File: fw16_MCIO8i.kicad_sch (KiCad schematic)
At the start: 12 parts

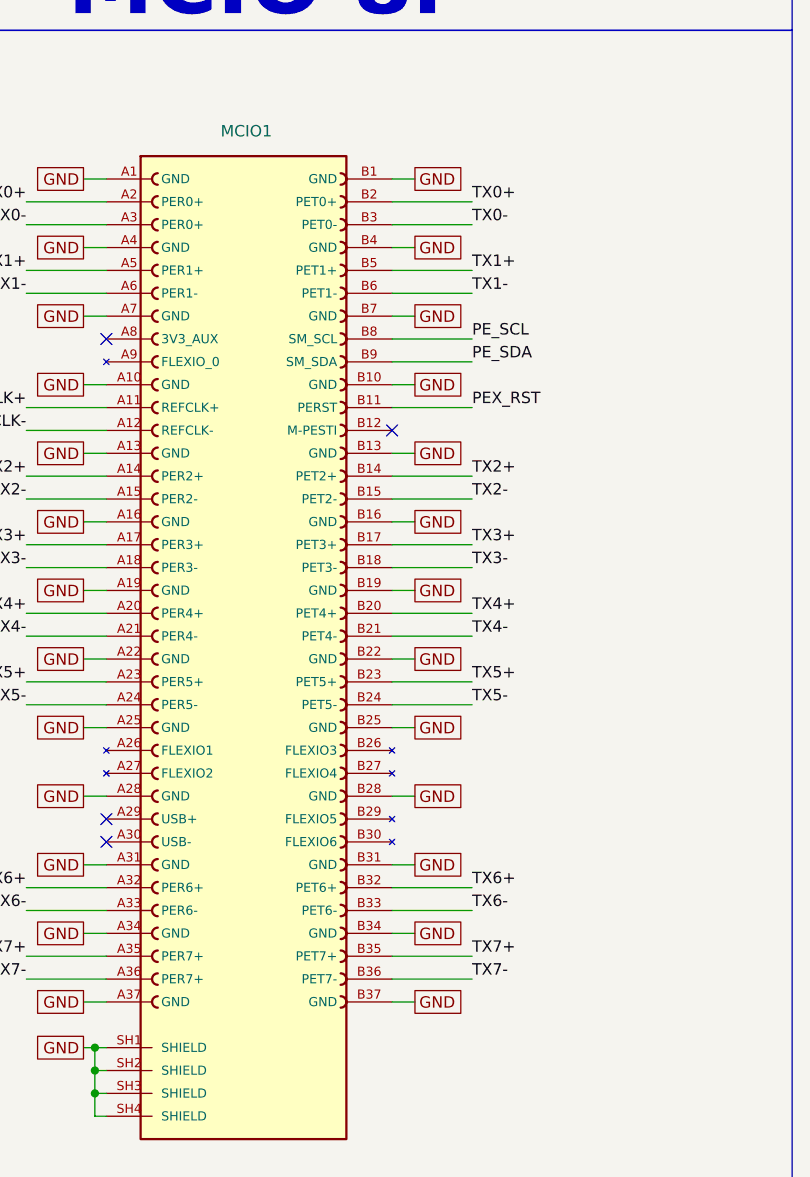
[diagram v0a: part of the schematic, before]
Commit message: Rerouted fxbeam
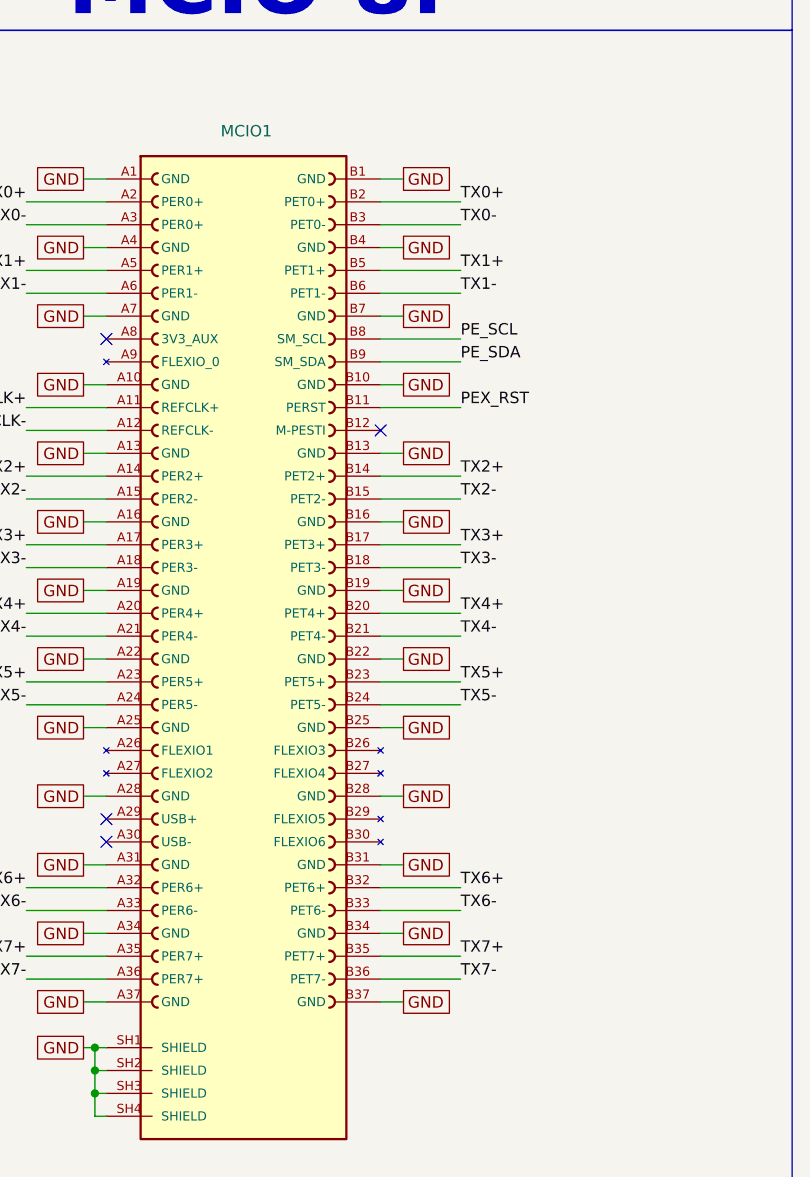
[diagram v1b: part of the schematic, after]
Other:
- moved on the sheet: MCIO1

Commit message: Fixed errors
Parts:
- C1: MPN (none) -> CL05A105KA5NQNC; PROD_ID (none) -> CAP-25565; Voltage (none) -> 16V
- EEPROM1: MPN (none) -> M24C32-FDW6TP
- FAN_L1, FAN_R1: CREATOR (none) -> ANA
- R1, R2: MPN (none) -> 0402WGF3303TCE; PROD_ID (none) -> RES-15407
- R50, R51: MPN (none) -> 0402WGF1002TCE; PROD_ID (none) -> RES-25567
- TP_POWER1: renamed from TP5; now left out of the parts list
- TP_SIGNAL1: renamed from TP3; now left out of the parts list
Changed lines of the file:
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@@
+		(polyline
+			(pts
+				(xy 76.2 162.56) (xy 78.74 162.56) (xy 78.74 184.15) (xy 76.2 184.15)
+			)
+			(stroke
+				(width 0)
+				(type dash)
+			)
+			(fill
+				(type none)
+			)
+		)
+	)
+	(rule_area
+		(polyline
+			(pts
+				(xy 34.29 245.11) (xy 36.83 245.11) (xy 36.83 247.65) (xy 34.29 247.65)
+			)
+			(stroke
+				(width 0)
+				(type dash)
+			)
+			(fill
+				(type none)
+			)
+		)
+	)
+	(rule_area
 		(polyline
 			(pts
 				(xy 76.2 40.64) (xy 76.2 140.97) (xy 78.74 140.97) (xy 78.74 40.64)
+			)
+			(stroke
+				(width 0)
+				(type dash)
+			)
+			(fill
+				(type none)
+			)
+		)
+	)
+	(rule_area
+		(polyline
+			(pts
+				(xy 76.2 241.3) (xy 78.74 241.3) (xy 78.74 278.13) (xy 76.2 278.13)
 			)
 			(stroke
@@
 			(pts
 				(xy 33.02 113.03) (xy 35.56 113.03) (xy 34.29 231.14) (xy 31.75 231.14)
-			)
-			(stroke
-				(width 0)
-				(type dash)
-			)
-			(fill
-				(type none)
-			)
-		)
-	)
-	(rule_area
-		(polyline
-			(pts
-				(xy 76.2 241.3) (xy 78.74 241.3) (xy 78.74 278.13) (xy 76.2 278.13)
-			)
-			(stroke
-				(width 0)
-				(type dash)
-			)
-			(fill
-				(type none)
-			)
-		)
-	)
-	(rule_area
-		(polyline
-			(pts
-				(xy 34.29 245.11) (xy 36.83 245.11) (xy 36.83 247.65) (xy 34.29 247.65)
-			)
-			(stroke
-				(width 0)
-				(type dash)
-			)
-			(fill
-				(type none)
-			)
-		)
-	)
-	(rule_area
-		(polyline
-			(pts
-				(xy 76.2 162.56) (xy 78.74 162.56) (xy 78.74 184.15) (xy 76.2 184.15)
 			)
 			(stroke
@@
 		(property "Temperature Coefficient" "±100ppm/°C"
 			(at 264.16 40.64 0)
+			(hide yes)
+			(effects
+				(font
+					(size 1.27 1.27)
+				)
+			)
+		)
+		(property "PROD_ID" "RES-25567"
+			(at 264.16 40.64 0)
+			(hide yes)
+			(effects
+				(font
+					(size 1.27 1.27)
+				)
+			)
+		)
+		(property "MPN" "0402WGF1002TCE"
+			(at 264.16 44.45 0)
 			(hide yes)
 			(effects
@@
 			)
 		)
+		(property "PROD_ID" "RES-25567"
+			(at 269.24 43.18 0)
+			(hide yes)
+			(effects
+				(font
+					(size 1.27 1.27)
+				)
+			)
+		)
+		(property "MPN" "0402WGF1002TCE"
+			(at 269.24 45.72 0)
+			(hide yes)
+			(effects
+				(font
+					(size 1.27 1.27)
+				)
+			)
+		)
 		(pin "1"
 		)
@@
 			)
 		)
+		(property "MPN" "M24C32-FDW6TP"
+			(at 219.71 48.26 0)
+			(hide yes)
+			(effects
+				(font
+					(size 1.27 1.27)
+				)
+			)
+		)
 		(pin "7"
 		)
@@
 		(unit 1)
 		(exclude_from_sim no)
-		(in_bom yes)
+		(in_bom no)
 		(on_board yes)
 		(dnp no)
-		(property "Reference" "TP3"
+		(property "Reference" "TP_SIGNAL1"
 			(at 36.068 102.87 0)
 			(effects
@@
 		(property "Value" "TestPoint_Small"
 			(at 32.512 101.092 0)
+			(hide yes)
 			(effects
 				(font
@@
 			(project "fw16_MCIO8i"
 				(path "/50f5fd03-67f8-43d1-8bfe-dca2cf908bf0"
-					(reference "TP3")
+					(reference "TP_SIGNAL1")
 					(unit 1)
 				)
@@
 			)
 		)
+		(property "CREATOR" "ANA"
+			(at 173.99 38.1 0)
+			(hide yes)
+			(effects
+				(font
+					(size 1.27 1.27)
+				)
+			)
+		)
+		(property "VERIFIER" ""
+			(at 173.99 38.1 0)
+			(hide yes)
+			(effects
+				(font
+					(size 1.27 1.27)
+				)
+			)
+		)
 		(pin "1"
 		)
@@
 		(property "MPN" "609-F33D-1A7H1-E7C04CT-ND"
 			(at 139.954 60.198 0)
+			(hide yes)
+			(effects
+				(font
+					(size 1.27 1.27)
+				)
+			)
+		)
+		(property "CREATOR" "ANA"
+			(at 139.7 38.1 0)
+			(hide yes)
+			(effects
+				(font
+					(size 1.27 1.27)
+				)
+			)
+		)
+		(property "VERIFIER" ""
+			(at 139.7 38.1 0)
 			(hide yes)
 			(effects
@@
 			)
 		)
+		(property "PROD_ID" "RES-15407"
+			(at 35.56 273.05 0)
+			(hide yes)
+			(effects
+				(font
+					(size 1.27 1.27)
+				)
+			)
+		)
+		(property "MPN" "0402WGF3303TCE"
+			(at 35.56 273.05 0)
+			(hide yes)
+			(effects
+				(font
+					(size 1.27 1.27)
+				)
+			)
+		)
 		(pin "1"
 		)
@@
 			)
 		)
+		(property "PROD_ID" "RES-15407"
+			(at 27.94 100.33 0)
+			(hide yes)
+			(effects
+				(font
+					(size 1.27 1.27)
+				)
+			)
+		)
+		(property "MPN" "0402WGF3303TCE"
+			(at 27.94 100.33 0)
+			(hide yes)
+			(effects
+				(font
+					(size 1.27 1.27)
+				)
+			)
+		)
 		(pin "1"
 		)
@@
 		(unit 1)
 		(exclude_from_sim no)
-		(in_bom yes)
+		(in_bom no)
 		(on_board yes)
 		(dnp no)
-		(property "Reference" "TP5"
-			(at 33.02 264.16 0)
+		(property "Reference" "TP_POWER1"
+			(at 31.242 266.7 0)
 			(effects
 				(font
@@
 		(property "Value" "TestPoint_Small"
 			(at 33.02 265.938 0)
+			(hide yes)
 			(effects
 				(font
@@
 			(project "fw16_MCIO8i"
 				(path "/50f5fd03-67f8-43d1-8bfe-dca2cf908bf0"
-					(reference "TP5")
+					(reference "TP_POWER1")
 					(unit 1)
 				)
@@
 		(on_board yes)
 		(dnp no)
-		(fields_autoplaced yes)
 		(property "Reference" "C1"
 			(at 246.38 34.2899 0)
@@
 			(hide yes)
 			(effects
+				(font
+					(size 1.27 1.27)
+				)
+			)
+		)
+		(property "PROD_ID" "CAP-25565"
+			(at 243.84 36.83 0)
+			(hide yes)
+			(effects
+				(font
+					(size 1.27 1.27)
+				)
+			)
+		)
+		(property "Voltage" "16V"
+			(at 243.84 36.83 0)
+			(hide yes)
+			(effects
+				(font
+					(size 1.27 1.27)
+				)
+			)
+		)
+		(property "MPN" "CL05A105KA5NQNC"
+			(at 248.92 41.91 0)
+			(hide yes)
+			(effects

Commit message: New routing
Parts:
- C1: MPN CL05A105KA5NQNC -> (none); PROD_ID CAP-25565 -> (none); Voltage 16V -> (none)
- EEPROM1: MPN M24C32-FDW6TP -> (none); now in the parts list
- IN1: renamed from FXBEAM1; value IN -> FXBEAM
- R1, R2: MPN 0402WGF3303TCE -> (none); PROD_ID RES-15407 -> (none)
- R50, R51: MPN 0402WGF1002TCE -> (none); PROD_ID RES-25567 -> (none)
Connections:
- net I2C_SCL: now also IN1.PD3 (I2C_DAT_ALW); no longer IN1.PF2 (I2C_INT_ALW)
- net I2C_SDA: now also IN1.PC3 (I2C_CLK_ALW); no longer IN1.PD3 (I2C_DAT_ALW)
- net PEX_RST: now also IN1.PF3 (PEX1_RST); no longer IN1.SA5 (PEX_RST#)
- net PE_SCL: now also IN1.PK1 (DDS_SDA); no longer IN1.PG3 (I2C_DAT_VS)
- net PE_SDA: now also IN1.PL2 (DDS_CLK); no longer IN1.PG2 (I2C_INT_VS)

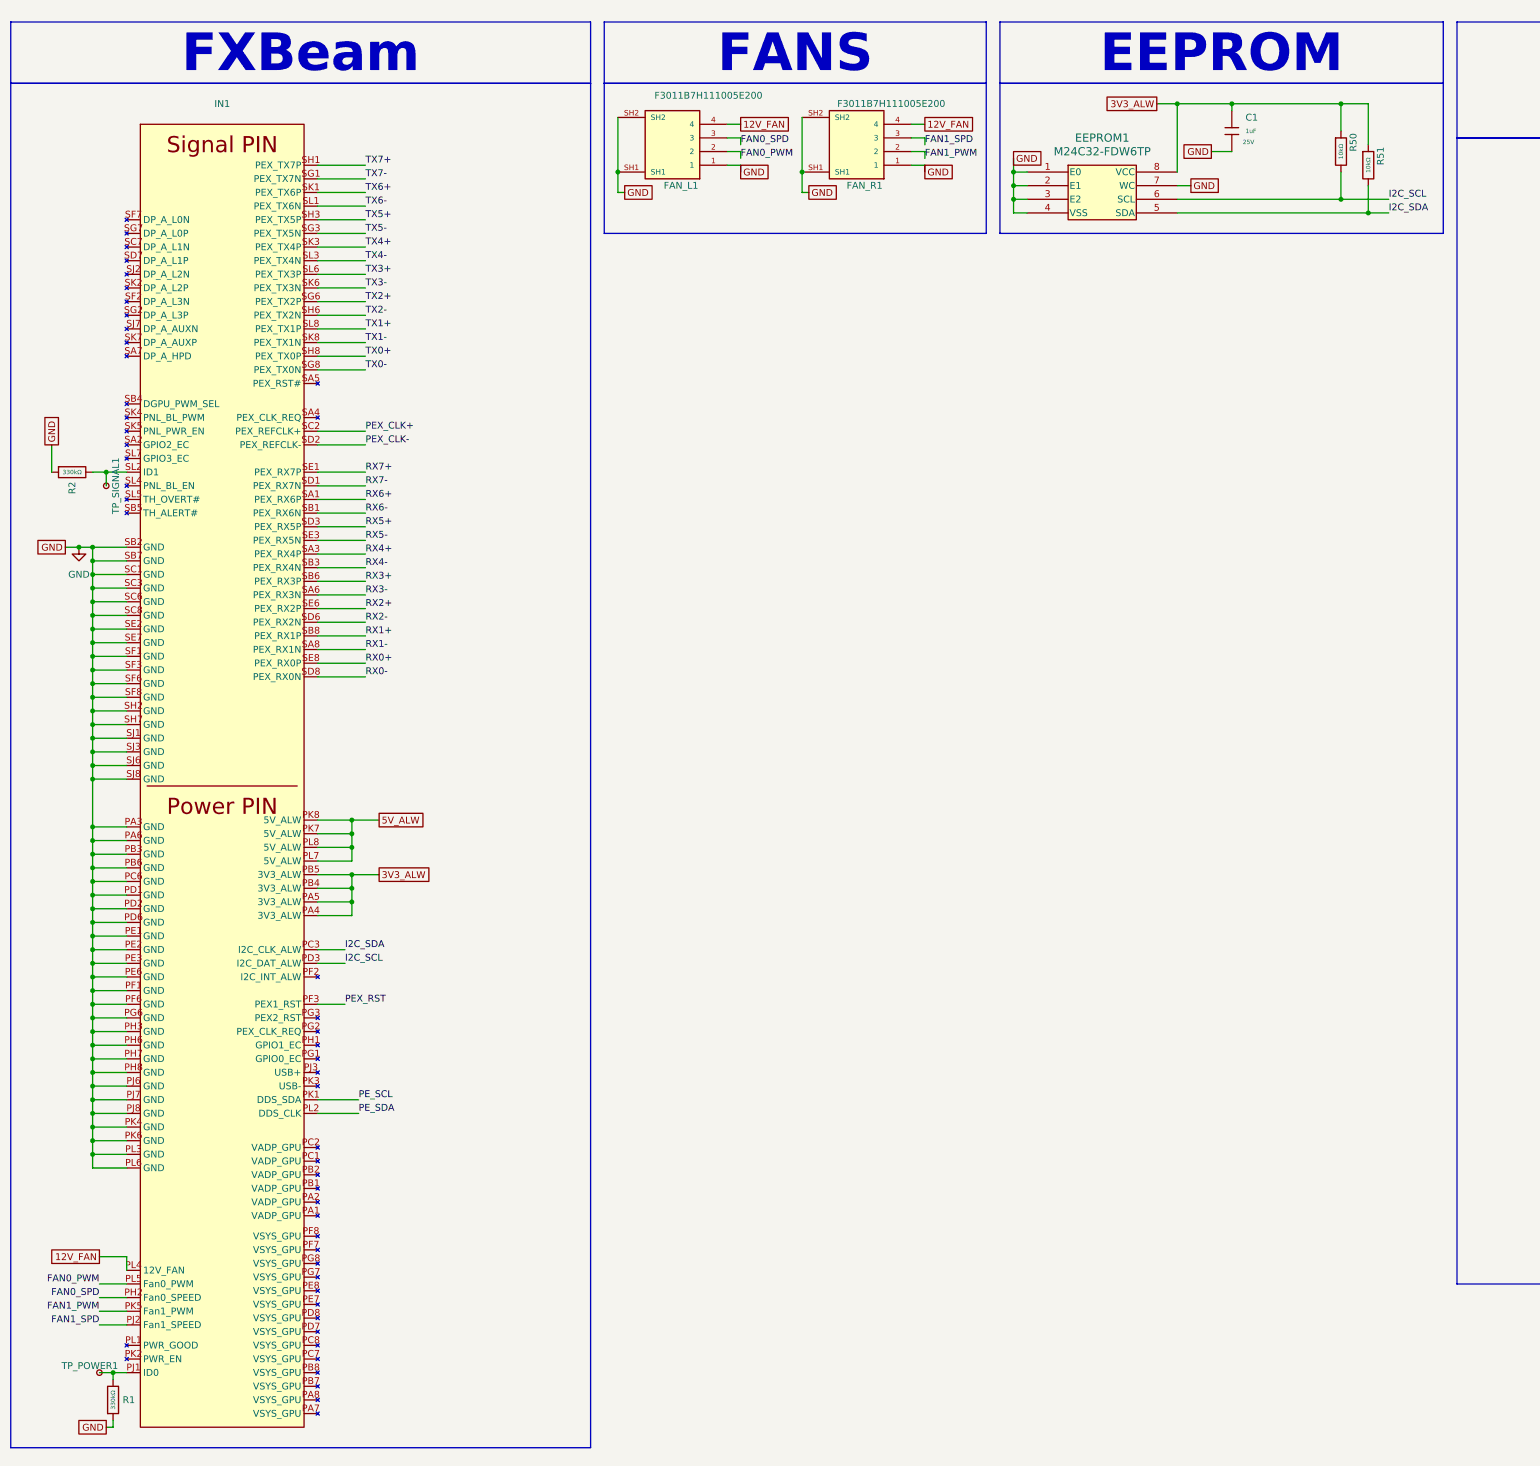
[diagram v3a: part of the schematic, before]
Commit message: diodes and jumpers
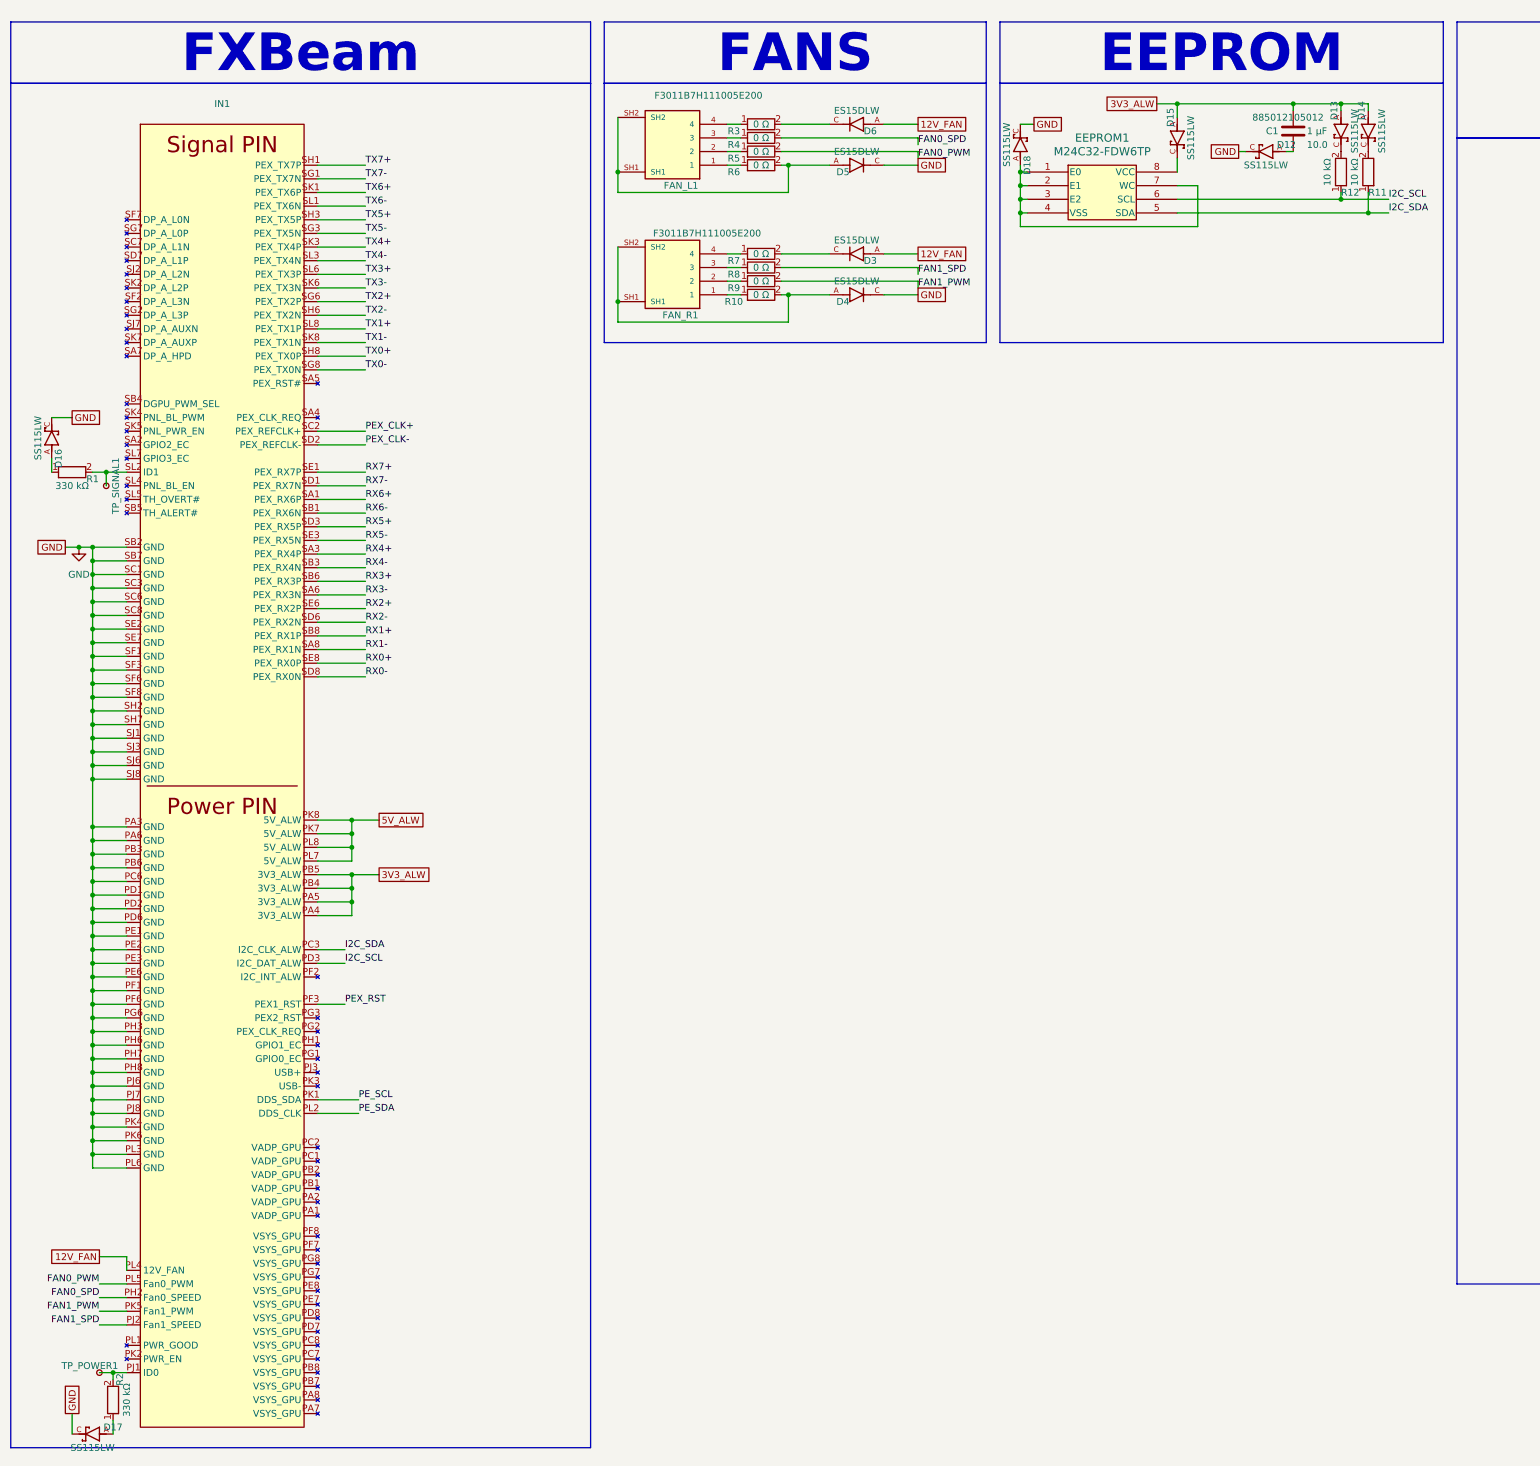
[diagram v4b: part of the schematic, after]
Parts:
- removed C1: 1uF, PCM_JLCPCB:C_0402, symbol PCM_JLCPCB-Capacitors:0402,1uF
- removed R1, R2: 330kΩ, PCM_JLCPCB:R_0402, symbol PCM_JLCPCB-Resistors:0402,330kΩ
- removed R50, R51: 10kΩ, PCM_JLCPCB:R_0402, symbol PCM_JLCPCB-Resistors:0402,10kΩ
- added C1: 0402_885012105012, capacitor:C_Wurth_WCAP-CSGP-0402, symbol capacitor:0402_885012105012
- added D12, D13, D14, D15, D16, D17, D18: SS115LW, diode:DIO_SS115LW, symbol diode:SS115LW
- added D3, D4, D5, D6: ES15DLW, fan-diode:SODFL3718X102N, symbol fan-diode:ES15DLW
- added R1, R2: 1206_R_560112132036, resistors:R_Wurth_WRIS-RSKS-1206_R, symbol resistor:1206_R_560112132036
- added R10, R3, R4, R5, R6, R7, R8, R9: 1206_R_560112132007, resistors:R_Wurth_WRIS-RSKS-1206_R, symbol resistor:1206_R_560112132007
- added R11, R12: 1206_R_560112132018, resistors:R_Wurth_WRIS-RSKS-1206_R, symbol resistor:1206_R_560112132018
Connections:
- net 12V_FAN: now also D3.A, D6.A; no longer FAN_L1.4, FAN_R1.4
- net 3V3_ALW: now also C1.1, D13.A, D14.A, D15.A; no longer EEPROM1.8 (VCC)
- net FAN0_PWM: now also R5.2; no longer FAN_L1.2
- net FAN0_SPD: now also R4.2; no longer FAN_L1.3
- net FAN1_PWM: now also R9.2; no longer FAN_R1.2
- net FAN1_SPD: now also R8.2; no longer FAN_R1.3
- net GND: now also D12.C, D16.C, D17.C, D18.C, D4.C, D5.C; no longer EEPROM1.1 (E0), EEPROM1.2 (E1), EEPROM1.3 (E2), EEPROM1.4 (VSS), EEPROM1.7 (WC), FAN_L1.1, FAN_L1.SH1, FAN_L1.SH2, FAN_R1.1, FAN_R1.SH1, FAN_R1.SH2
- net I2C_SCL: now also R12.1
- net I2C_SDA: now also R11.1
- net at IN1.PJ1 (ID0), TP_POWER1.1: now also R2.2
- net at IN1.SL2 (ID1), TP_SIGNAL1.1: now also R1.2
- new net: D3.C, R7.2
- new net: FAN_L1.4, R3.1
- new net: D6.C, R3.2
- new net: D14.C, R11.2
- new net: FAN_L1.3, R4.1
- new net: D17.A, R2.1
- new net: FAN_L1.1, R6.1
- new net: D5.A, FAN_L1.SH1, FAN_L1.SH2, R6.2
- new net: D16.A, R1.1
- new net: C1.2, D12.A
- new net: FAN_R1.3, R8.1
- new net: D18.A, EEPROM1.1 (E0), EEPROM1.2 (E1), EEPROM1.3 (E2), EEPROM1.4 (VSS), EEPROM1.7 (WC)
- new net: D15.C, EEPROM1.8 (VCC)
- new net: D13.C, R12.2
- new net: FAN_R1.1, R10.1
- new net: FAN_R1.2, R9.1
- new net: FAN_R1.4, R7.1
- new net: D4.A, FAN_R1.SH1, FAN_R1.SH2, R10.2
- new net: FAN_L1.2, R5.1
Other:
- moved on the sheet: FAN_R1

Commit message: README and cleanup
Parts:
- removed D12, D13, D14, D15, D18: SS115LW, diode:DIO_SS115LW, symbol diode:SS115LW
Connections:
- net 3V3_ALW: now also EEPROM1.8 (VCC), R11.2, R12.2
- net GND: now also C1.2, EEPROM1.1 (E0), EEPROM1.2 (E1), EEPROM1.3 (E2), EEPROM1.4 (VSS), EEPROM1.7 (WC)
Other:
- moved on the sheet: C1, R12
